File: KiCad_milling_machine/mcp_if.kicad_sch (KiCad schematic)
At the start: 11 parts

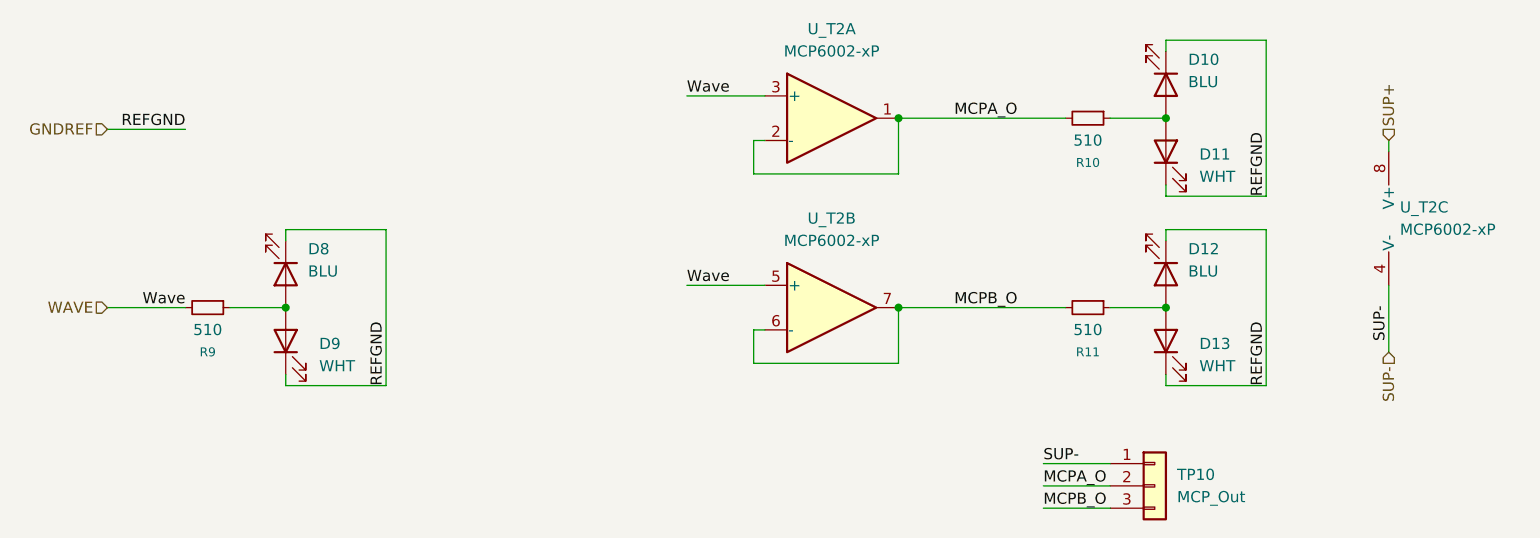
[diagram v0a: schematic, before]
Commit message: Removed Switch
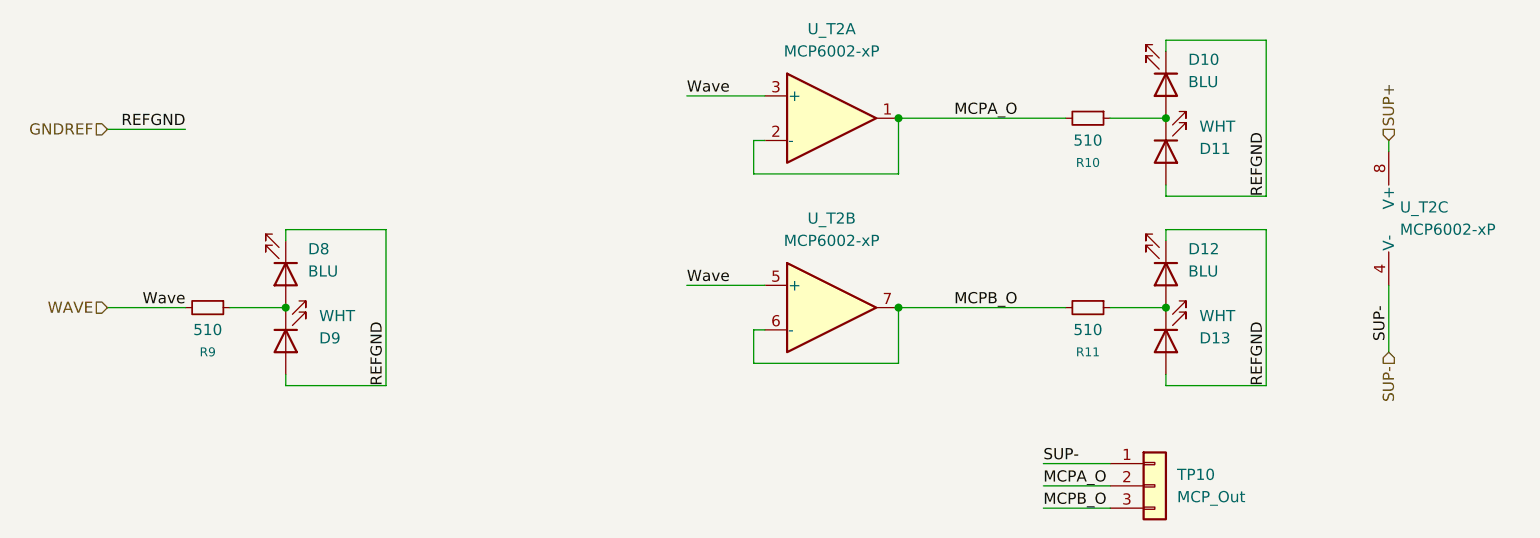
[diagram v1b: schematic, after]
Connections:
- net GNDREF: now also D11.2 (A), D13.2 (A), D9.2 (A); no longer D11.1 (K), D13.1 (K), D9.1 (K)
- net at D8.2 (A), R9.1: now also D9.1 (K); no longer D9.2 (A)
- net at D12.2 (A), R11.1: now also D13.1 (K); no longer D13.2 (A)
- net at D10.2 (A), R10.1: now also D11.1 (K); no longer D11.2 (A)
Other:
- moved on the sheet: D11, D13, D9
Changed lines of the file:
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@@
 		(lib_id "Device:LED")
 		(at 48.26 62.23 90)
+		(mirror x)
 		(unit 1)
 		(exclude_from_sim no)
@@
 		(on_board yes)
 		(dnp no)
-		(fields_autoplaced yes)
 		(property "Reference" "D9"
-			(at 52.07 62.5474 90)
+			(at 52.07 61.9126 90)
 			(effects
 				(font
@@
 		)
 		(property "Value" "WHT"
-			(at 52.07 65.0874 90)
+			(at 52.07 59.3726 90)
 			(effects
 				(font
@@
 		(lib_id "Device:LED")
 		(at 148.59 40.64 90)
+		(mirror x)
 		(unit 1)
 		(exclude_from_sim no)
@@
 		(on_board yes)
 		(dnp no)
-		(fields_autoplaced yes)
 		(property "Reference" "D11"
-			(at 152.4 40.9574 90)
+			(at 152.4 40.3226 90)
 			(effects
 				(font
@@
 		)
 		(property "Value" "WHT"
-			(at 152.4 43.4974 90)
+			(at 152.4 37.7826 90)
 			(effects
 				(font
@@
 		(lib_id "Device:LED")
 		(at 148.59 62.23 90)
+		(mirror x)
 		(unit 1)
 		(exclude_from_sim no)
@@
 		(on_board yes)
 		(dnp no)
-		(fields_autoplaced yes)
 		(property "Reference" "D13"
-			(at 152.4 62.5474 90)
+			(at 152.4 61.9126 90)
 			(effects
 				(font
@@
 		)
 		(property "Value" "WHT"
-			(at 152.4 65.0874 90)
-			(effects
-				(font
+			(at 152.4 59.3726 90)
+			(effects
+				(font

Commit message: grounded LEDs to allow for sufficient voltage blinking difference
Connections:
- net GNDREF: no longer D10.1 (K), D11.2 (A), D12.1 (K), D13.2 (A), D8.1 (K), D9.2 (A)
- net at D8.2 (A), R9.1: now also D9.2 (A); no longer D9.1 (K)
- net at D12.2 (A), R11.1: now also D13.2 (A); no longer D13.1 (K)
- net at D10.2 (A), R10.1: now also D11.2 (A); no longer D11.1 (K)
- new net GND: D10.1 (K), D11.1 (K), D12.1 (K), D13.1 (K), D8.1 (K), D9.1 (K)
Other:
- moved on the sheet: D11, D13, D9
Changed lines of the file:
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@@
+	)
+	(junction
+		(at 48.26 58.42)
+		(diameter 0)
+		(color 0 0 0 0)
+	)
+	(junction
+		(at 148.59 58.42)
+		(diameter 0)
+		(color 0 0 0 0)
+	)
+	(junction
+		(at 118.11 58.42)
+		(diameter 0)
+		(color 0 0 0 0)
+	)
+	(junction
+		(at 59.69 67.31)
+		(diameter 0)
+		(color 0 0 0 0)
+	)
+	(junction
+		(at 160.02 67.31)
+		(diameter 0)
+		(color 0 0 0 0)
 	)
 	(junction
@@
 	)
 	(junction
-		(at 48.26 58.42)
+		(at 160.02 45.72)
 		(diameter 0)
 		(color 0 0 0 0)
 	)
-	(junction
-		(at 118.11 58.42)
-		(diameter 0)
-		(color 0 0 0 0)
-	)
-	(junction
-		(at 148.59 58.42)
-		(diameter 0)
-		(color 0 0 0 0)
-	)
 	(wire
 		(pts
@@
 			(width 0)
 			(type default)
-		)
-	)
-	(label "REFGND"
-		(at 59.69 67.31 90)
-		(effects
-			(font
-				(size 1.27 1.27)
-			)
-			(justify left bottom)
-		)
-	)
-	(label "REFGND"
-		(at 160.02 45.72 90)
-		(effects
-			(font
-				(size 1.27 1.27)
-			)
-			(justify left bottom)
 		)
 	)
@@
 	(label "SUP-"
 		(at 173.99 62.23 90)
-		(effects
-			(font
-				(size 1.27 1.27)
-			)
-			(justify left bottom)
-		)
-	)
-	(label "REFGND"
-		(at 160.02 67.31 90)
 		(effects
 			(font
@@
 	(symbol
 		(lib_id "Device:LED")
-		(at 48.26 62.23 90)
+		(at 48.26 62.23 270)
 		(mirror x)
 		(unit 1)
@@
 		(dnp no)
 		(property "Reference" "D9"
-			(at 52.07 61.9126 90)
+			(at 44.45 62.5474 90)
 			(effects
 				(font
@@
 		)
 		(property "Value" "WHT"
-			(at 52.07 59.3726 90)
+			(at 44.45 65.0874 90)
 			(effects
 				(font
@@
 				(path "/57b9e980-cd8f-44e4-af61-2cbd5bb30325/66abbfc5-c7ee-42ee-8f01-bf5211a4ea1c"
 					(reference "D9")
+					(unit 1)
+				)
+			)
+		)
+	)
+	(symbol
+		(lib_id "power:GND")
+		(at 59.69 67.31 0)
+		(unit 1)
+		(exclude_from_sim no)
+		(in_bom yes)
+		(on_board yes)
+		(dnp no)
+		(fields_autoplaced yes)
+		(property "Reference" "#PWR012"
+			(at 59.69 73.66 0)
+			(effects
+				(font
+					(size 1.27 1.27)
+				)
+				(hide yes)
+			)
+		)
+		(property "Value" "GND"
+			(at 59.69 72.39 0)
+			(effects
+				(font
+					(size 1.27 1.27)
+				)
+			)
+		)
+		(property "Footprint" ""
+			(at 59.69 67.31 0)
+			(effects
+				(font
+					(size 1.27 1.27)
+				)
+				(hide yes)
+			)
+		)
+		(property "Datasheet" ""
+			(at 59.69 67.31 0)
+			(effects
+				(font
+					(size 1.27 1.27)
+				)
+				(hide yes)
+			)
+		)
+		(property "Description" "Power symbol creates a global label with name \"GND\" , ground"
+			(at 59.69 67.31 0)
+			(effects
+				(font
+					(size 1.27 1.27)
+				)
+				(hide yes)
+			)
+		)
+		(pin "1"
+		)
+		(instances
+			(project "ChipTester_354"
+				(path "/57b9e980-cd8f-44e4-af61-2cbd5bb30325/66abbfc5-c7ee-42ee-8f01-bf5211a4ea1c"
+					(reference "#PWR012")
 					(unit 1)
 				)
@@
 	)
 	(symbol
+		(lib_id "power:GND")
+		(at 160.02 67.31 90)
+		(unit 1)
+		(exclude_from_sim no)
+		(in_bom yes)
+		(on_board yes)
+		(dnp no)
+		(fields_autoplaced yes)
+		(property "Reference" "#PWR014"
+			(at 166.37 67.31 0)
+			(effects
+				(font
+					(size 1.27 1.27)
+				)
+				(hide yes)
+			)
+		)
+		(property "Value" "GND"
+			(at 163.83 67.3099 90)
+			(effects
+				(font
+					(size 1.27 1.27)
+				)
+				(justify right)
+			)
+		)
+		(property "Footprint" ""
+			(at 160.02 67.31 0)
+			(effects
+				(font
+					(size 1.27 1.27)
+				)
+				(hide yes)
+			)
+		)
+		(property "Datasheet" ""
+			(at 160.02 67.31 0)
+			(effects
+				(font
+					(size 1.27 1.27)
+				)
+				(hide yes)
+			)
+		)
+		(property "Description" "Power symbol creates a global label with name \"GND\" , ground"
+			(at 160.02 67.31 0)
+			(effects
+				(font
+					(size 1.27 1.27)
+				)
+				(hide yes)
+			)
+		)
+		(pin "1"
+		)
+		(instances
+			(project "ChipTester_354"
+				(path "/57b9e980-cd8f-44e4-af61-2cbd5bb30325/66abbfc5-c7ee-42ee-8f01-bf5211a4ea1c"
+					(reference "#PWR014")
+					(unit 1)
+				)
+			)
+		)
+	)
+	(symbol
 		(lib_id "Device:LED")
-		(at 148.59 40.64 90)
+		(at 148.59 40.64 270)
 		(mirror x)
 		(unit 1)
@@
 		(dnp no)
 		(property "Reference" "D11"
-			(at 152.4 40.3226 90)
+			(at 144.78 40.9574 90)
 			(effects
 				(font
@@
 		)
 		(property "Value" "WHT"
-			(at 152.4 37.7826 90)
+			(at 144.78 43.4974 90)
 			(effects
 				(font
@@
 				(path "/57b9e980-cd8f-44e4-af61-2cbd5bb30325/66abbfc5-c7ee-42ee-8f01-bf5211a4ea1c"
 					(reference "D11")
+					(unit 1)
+				)
+			)
+		)
+	)
+	(symbol
+		(lib_id "power:GND")
+		(at 160.02 45.72 90)
+		(unit 1)
+		(exclude_from_sim no)
+		(in_bom yes)
+		(on_board yes)
+		(dnp no)
+		(fields_autoplaced yes)
+		(property "Reference" "#PWR013"
+			(at 166.37 45.72 0)
+			(effects
+				(font
+					(size 1.27 1.27)
+				)
+				(hide yes)
+			)
+		)
+		(property "Value" "GND"
+			(at 163.83 45.7199 90)
+			(effects
+				(font
+					(size 1.27 1.27)
+				)
+				(justify right)
+			)
+		)
+		(property "Footprint" ""
+			(at 160.02 45.72 0)
+			(effects
+				(font
+					(size 1.27 1.27)
+				)
+				(hide yes)
+			)
+		)
+		(property "Datasheet" ""
+			(at 160.02 45.72 0)
+			(effects
+				(font
+					(size 1.27 1.27)
+				)
+				(hide yes)
+			)
+		)
+		(property "Description" "Power symbol creates a global label with name \"GND\" , ground"
+			(at 160.02 45.72 0)
+			(effects
+				(font
+					(size 1.27 1.27)
+				)
+				(hide yes)
+			)
+		)
+		(pin "1"
+		)
+		(instances
+			(project "ChipTester_354"
+				(path "/57b9e980-cd8f-44e4-af61-2cbd5bb30325/66abbfc5-c7ee-42ee-8f01-bf5211a4ea1c"
+					(reference "#PWR013")
 					(unit 1)
 				)
@@
 	(symbol
 		(lib_id "Device:LED")
-		(at 148.59 62.23 90)
+		(at 148.59 62.23 270)
 		(mirror x)
 		(unit 1)
@@
 		(dnp no)
 		(property "Reference" "D13"
-			(at 152.4 61.9126 90)
+			(at 144.78 62.5474 90)
 			(effects
 				(font
@@
 		)
 		(property "Value" "WHT"
-			(at 152.4 59.3726 90)
-			(effects
-				(font
+			(at 144.78 65.0874 90)
+			(effects
+				(font
